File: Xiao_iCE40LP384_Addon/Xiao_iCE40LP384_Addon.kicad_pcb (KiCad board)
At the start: 2 copper layers, 17.8 x 21 mm, 26 parts, among them J1 Conn_01x07_Pin, J2 Conn_01x07_Pin, SW1 SW_Push, U1 ICE40LP384-SG32, U2 ADP322ACPZ-145-R7, U4 XIAO-SAMD21-SMD

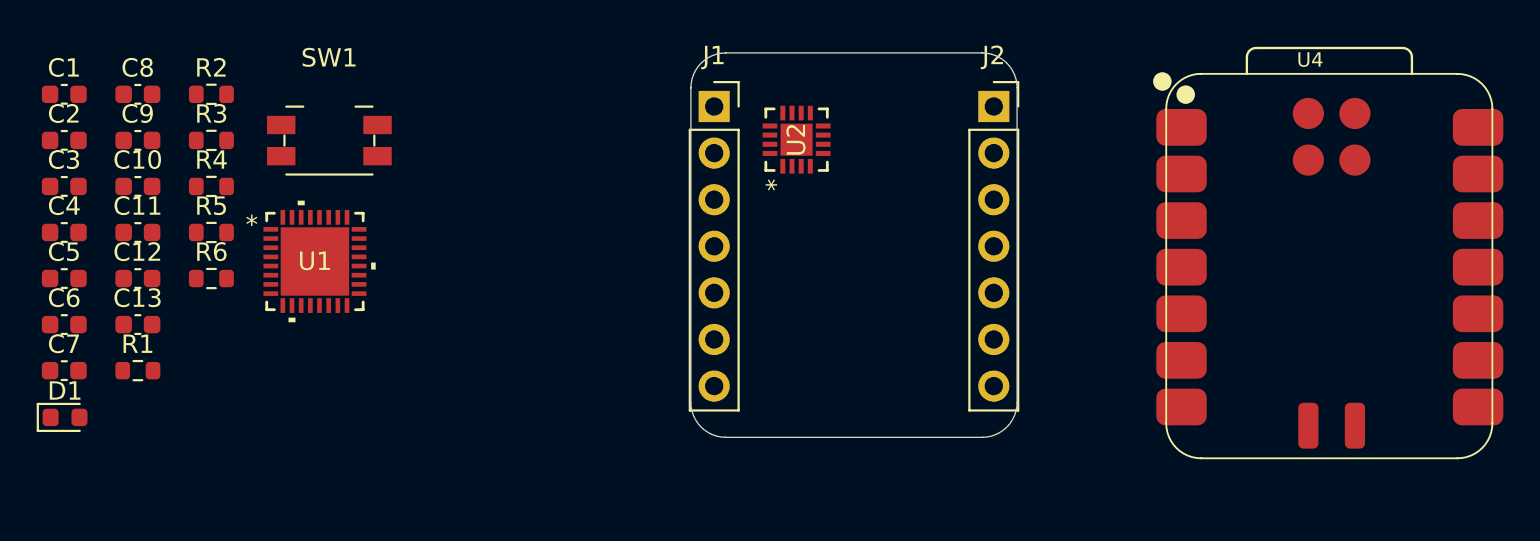
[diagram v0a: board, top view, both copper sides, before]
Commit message: Finished most of the XIAO floorplan, need to route FPGA caps
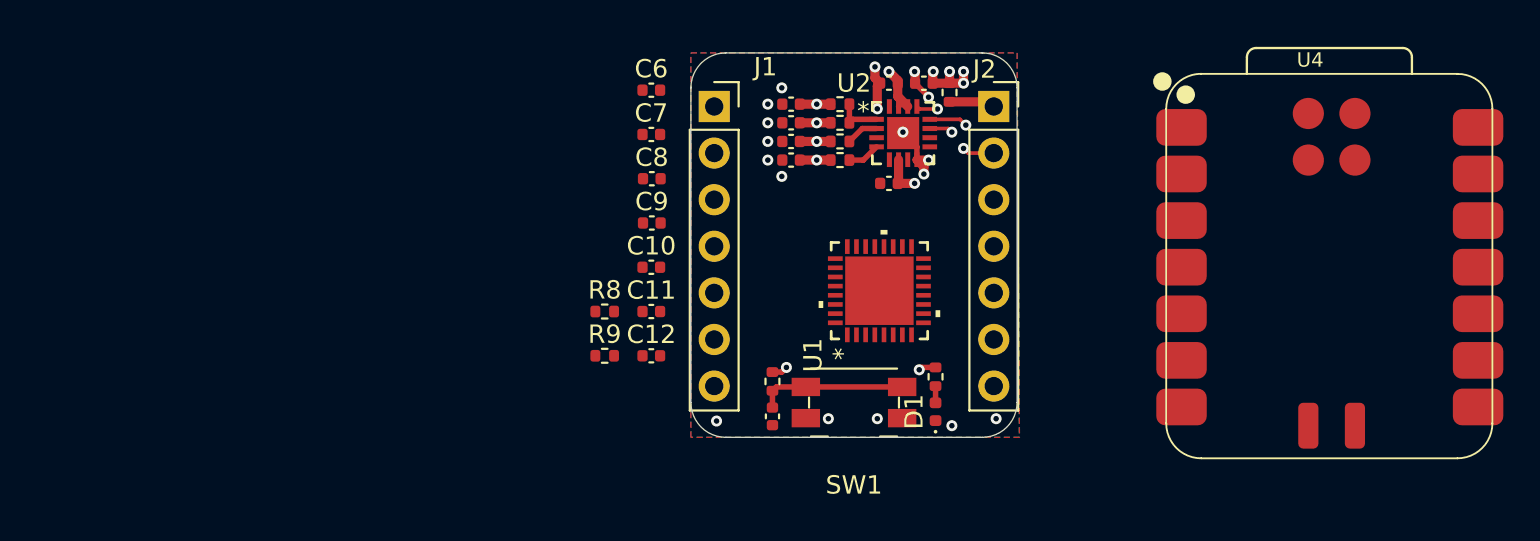
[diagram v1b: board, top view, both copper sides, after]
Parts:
- added C14: 1u, Capacitor_SMD:C_0402_1005Metric, F.Cu at (108.6, 52.1)
- added C15: 100n, Capacitor_SMD:C_0402_1005Metric, F.Cu at (102.2, 70.2)
- added R7: 10k, Resistor_SMD:R_0402_1005Metric, F.Cu at (102.2, 68.3)
- added R8: 0, Resistor_SMD:R_0402_1005Metric, F.Cu at (93.1, 64.5)
- added R9: 0, Resistor_SMD:R_0402_1005Metric, F.Cu at (93.1, 66.9)
- C1, C10, C11, C12, C2, C3, C4, C5, C6, C7, C8, C9: footprint Capacitor_SMD:C_0603_1608Metric -> Capacitor_SMD:C_0402_1005Metric
- C13: value 100n -> 1u; footprint Capacitor_SMD:C_0603_1608Metric -> Capacitor_SMD:C_0402_1005Metric
- D1: footprint LED_SMD:LED_0603_1608Metric -> LED_SMD:LED_0402_1005Metric
- R1, R2, R3, R4: footprint Resistor_SMD:R_0603_1608Metric -> Resistor_SMD:R_0402_1005Metric
- R5: value 1000 -> 0; footprint Resistor_SMD:R_0603_1608Metric -> Resistor_SMD:R_0402_1005Metric
- R6: value 10k -> 1000; footprint Resistor_SMD:R_0603_1608Metric -> Resistor_SMD:R_0402_1005Metric
- moved D1 47.5 mm to (111.1, 70.0), turned to 90 degrees
- moved C1 46.9 mm to (110.5, 52.1), turned to 180 degrees
- moved C13 41.7 mm to (108.6, 57.5), turned to 180 degrees
- moved R5 41.0 mm to (111.9, 52.6), turned to 90 degrees
- moved C5 40.3 mm to (103.3, 55.2), turned to 180 degrees
- moved C4 40.1 mm to (103.3, 54.2), turned to 180 degrees
- moved R1 40.0 mm to (105.9, 56.3), turned to 180 degrees
- moved C3 39.9 mm to (103.3, 53.2), turned to 180 degrees
- moved R6 39.8 mm to (111.1, 68.1), turned to -90 degrees
- moved C2 39.6 mm to (103.3, 56.3), turned to 180 degrees
- moved C7 34.5 mm to (95.6, 54.9)
- moved C6 34.5 mm to (95.6, 52.5)
- moved R4 34.4 mm to (105.9, 55.2), turned to 180 degrees
- moved R3 34.3 mm to (105.9, 54.2), turned to 180 degrees
- moved R2 34.3 mm to (105.9, 53.2), turned to 180 degrees
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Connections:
- C13 pad 1: /CRESET_B -> /5V0
- J1 pad 1: unconnected-(J1-Pin_1-Pad1) -> /D0
- J1 pad 2: unconnected-(J1-Pin_2-Pad2) -> /D1
- J1 pad 3: unconnected-(J1-Pin_3-Pad3) -> /D2
- J1 pad 4: unconnected-(J1-Pin_4-Pad4) -> /D3
- J1 pad 5: unconnected-(J1-Pin_5-Pad5) -> /D4_SDA
- J1 pad 6: unconnected-(J1-Pin_6-Pad6) -> /D5_SCL
- J1 pad 7: unconnected-(J1-Pin_7-Pad7) -> /D6_RX
- J2 pad 1: unconnected-(J2-Pin_1-Pad1) -> /5V0_IN
- J2 pad 2: unconnected-(J2-Pin_2-Pad2) -> /GND
- J2 pad 3: unconnected-(J2-Pin_3-Pad3) -> /3V3_IN
- J2 pad 4: unconnected-(J2-Pin_4-Pad4) -> /D10_MISO
- J2 pad 5: unconnected-(J2-Pin_5-Pad5) -> /D9_MOSI
- J2 pad 6: unconnected-(J2-Pin_6-Pad6) -> /D8_SCK
- J2 pad 7: unconnected-(J2-Pin_7-Pad7) -> /D7_TX
- R5 pad 1: /5V0 -> /5V0_IN
- R5 pad 2: Net-(D1-A) -> /5V0
- R6 pad 1: /VCCIO -> /5V0
- R6 pad 2: /CRESET_B -> Net-(D1-A)
- U1 pad 10: unconnected-(U1-CRESET_B-Pad10) -> /CRESET_B
- U1 pad 11: unconnected-(U1-CDONE-Pad11) -> /CDONE
- U1 pad 12: unconnected-(U1-IOB_24_SDO-Pad12) -> /D9_MOSI
- U1 pad 13: unconnected-(U1-IOB_25_SDI-Pad13) -> /D10_MISO
- U1 pad 15: unconnected-(U1-IOB_26_SCK-Pad15) -> /D8_SCK
- U1 pad 19: unconnected-(U1-IOR_35_GBIN3-Pad19) -> /D5_SCL
- U1 pad 20: unconnected-(U1-IOR_36_GBIN2-Pad20) -> /D4_SDA
- U1 pad 29: unconnected-(U1-IOT_49_GBIN0-Pad29) -> /D2
- U1 pad 30: unconnected-(U1-IOT_50_GBIN1-Pad30) -> /D3
- U1 pad 6: unconnected-(U1-IOL_4B_GBIN7-Pad6) -> /D7_TX
- U1 pad 7: unconnected-(U1-IOL_5A_GBIN6-Pad7) -> /D6_RX
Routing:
- net /5V0: track 0.00 -> 9.53 mm, vias 0 -> 7
- net /GND: track 0.00 -> 9.25 mm, vias 0 -> 19
- net /CRESET_B: track 0.00 -> 8.07 mm
- net /3V3: track 0.00 -> 2.58 mm
- net /VCCIO: track 0.00 -> 2.54 mm, vias 0 -> 2
- net /5V0_IN: track 0.00 -> 2.52 mm
- net /EN2: track 0.00 -> 2.10 mm, vias 0 -> 1
- net /1V2: track 0.00 -> 1.78 mm
- net /2V5: track 0.00 -> 1.77 mm
- net /VCC_SPI: track 0.00 -> 1.68 mm, vias 0 -> 1
- net /VCC: track 0.00 -> 1.68 mm, vias 0 -> 1
- net /VPP: track 0.00 -> 1.52 mm, vias 0 -> 1
- net /EN3: track 0.00 -> 1.29 mm, vias 0 -> 1
- net /EN1: track 0.00 -> 1.18 mm, vias 0 -> 1
- net Net-(D1-A): track 0.00 -> 0.91 mm
- added copper zone on In2.Cu, net /5V0
- added copper zone on B.Cu, net /GND
- added copper zone on F.Cu, net /GND
- added copper zone on In1.Cu, net /GND
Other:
- copper layers 2 -> 4

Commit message: XIAO done, as long as no problems come up during prototype testing
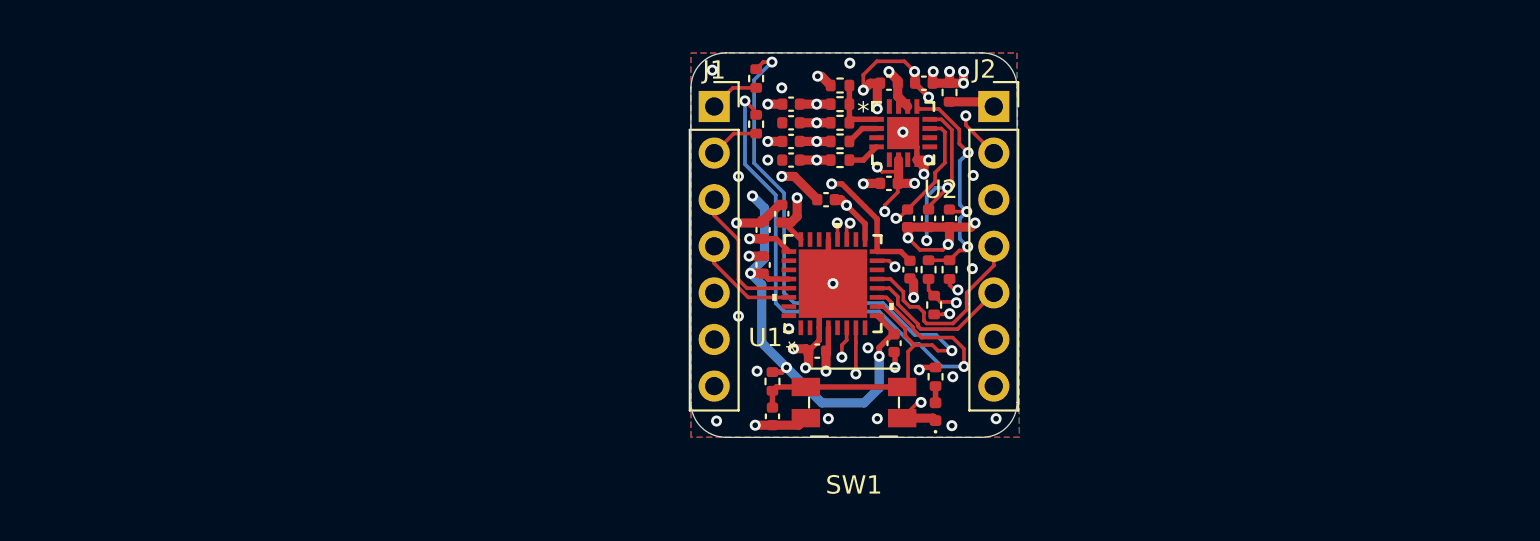
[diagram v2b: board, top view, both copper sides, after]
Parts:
- removed U4: XIAO-SAMD21-SMD, XIAO Footprints and Symbols:XIAO-RP2040-SMD
- added C16: 100n, Capacitor_SMD:C_0402_1005Metric, F.Cu at (109.6, 59.4)
- added C17: 100n, Capacitor_SMD:C_0402_1005Metric, F.Cu at (111.9, 59.4)
- added C18: 100n, Capacitor_SMD:C_0402_1005Metric, F.Cu at (110.7, 59.4)
- added R10: 10k, Resistor_SMD:R_0402_1005Metric, F.Cu at (102.2, 68.3)
- added R11: 10k, Resistor_SMD:R_0402_1005Metric, F.Cu at (111.0, 64.2)
- added R12: 10k, Resistor_SMD:R_0402_1005Metric, F.Cu at (110.7, 62.2)
- added R13: 10k, Resistor_SMD:R_0402_1005Metric, F.Cu at (111.9, 62.2)
- R6: value 1000 -> 0
- R7: value 10k -> 1000
- moved R6 16.7 mm to (105.9, 52.2), turned to 0 degrees
- moved C8 16.0 mm to (108.9, 66.2), turned to -90 degrees
- moved R8 15.1 mm to (101.3, 51.8), turned to -90 degrees
- moved R9 15.1 mm to (101.3, 54.3), turned to -90 degrees
- moved C11 14.3 mm to (109.7, 62.2), turned to -90 degrees
- moved C9 11.4 mm to (104.7, 66.7), turned to 180 degrees
- moved C12 10.5 mm to (102.7, 59.2), turned to 90 degrees
- moved C7 10.2 mm to (105.2, 58.4), turned to 180 degrees
- moved C6 9.76 mm to (101.7, 60.1), turned to 90 degrees
- moved R7 8.89 mm to (111.1, 68.1)
- moved C10 6.10 mm to (101.7, 62.0), turned to 90 degrees
- moved U1 2.56 mm to (105.5, 63.0)
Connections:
- R6 pad 1: /5V0 -> /3V3_IN
- R6 pad 2: Net-(D1-A) -> /3V3
- R7 pad 1: /VCCIO -> /5V0
- R7 pad 2: /CRESET_B -> Net-(D1-A)
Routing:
- net /VCCIO: track 2.54 -> 63.1 mm, vias 2 -> 7
- net /GND: track 9.25 -> 48.0 mm, vias 19 -> 41
- net /CRESET_B: track 8.07 -> 41.1 mm, vias 0 -> 2
- net /CDONE: track 0.00 -> 31.4 mm, vias 0 -> 2
- net /5V0: track 9.53 -> 34.4 mm, vias 7 -> 10
- net /3V3_IN: track 0.00 -> 15.9 mm, vias 0 -> 1
- net /EN3: track 1.29 -> 15.6 mm, vias 1 -> 2
- net /EN2: track 2.10 -> 14.5 mm, vias 1 -> 3
- net /EN1: track 1.18 -> 13.5 mm, vias 1 -> 3
- net /VCC_SPI: track 1.68 -> 13.7 mm, vias 1 -> 2
- net /D5_SCL: track 0.00 -> 11.5 mm, vias 0 -> 1
- net /D6_RX: track 0.00 -> 11.2 mm, vias 0 -> 1
- net /D10_MISO: track 0.00 -> 10.8 mm
- net /D7_TX: track 0.00 -> 10.6 mm, vias 0 -> 1
- net /D4_SDA: track 0.00 -> 9.85 mm, vias 0 -> 1
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- added copper zone on In2.Cu, net /VCCIO

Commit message: Noted lack of 5V tolerance
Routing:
- net /GND: track 48.0 -> 48.4 mm, vias 41 -> 42
- net /VCCIO: vias 7 -> 9
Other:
- board text added: "Not 5V Tolerant!"
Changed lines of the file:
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@@
 	(paper "A4")
 	(layers
-		(0 "F.Cu" signal)
-		(4 "In1.Cu" signal)
-		(6 "In2.Cu" signal)
-		(2 "B.Cu" signal)
+		(0 "F.Cu" mixed)
+		(4 "In1.Cu" power)
+		(6 "In2.Cu" mixed)
+		(2 "B.Cu" power)
 		(9 "F.Adhes" user "F.Adhesive")
 		(11 "B.Adhes" user "B.Adhesive")
@@
 		(layer "Edge.Cuts")
 	)
+	(gr_text "Not 5V Tolerant!"
+		(at 106.7562 51.5874 0)
+		(layer "F.SilkS")
+		(effects
+			(font
+				(size 0.8 0.8)
+				(thickness 0.1)
+			)
+			(justify bottom)
+		)
+	)
 	(segment
 		(start 108.585 51.435)
@@
 	)
 	(via
+		(at 114.5286 51.5874)
+		(size 0.6)
+		(drill 0.3)
+		(layers "F.Cu" "B.Cu")
+		(free yes)
+		(net 2)
+	)
+	(via
 		(at 113.284 59.69)
 		(size 0.6)
@@
 	)
 	(segment
+		(start 102.743 52.324)
+		(end 102.87 52.451)
+		(width 0.2)
+		(layer "B.Cu")
+		(net 2)
+	)
+	(segment
+		(start 102.743 52.324)
+		(end 102.87 52.451)
+		(width 0.2)
+		(layer "In1.Cu")
+		(net 2)
+	)
+	(segment
 		(start 100.9904 60.551)
 		(end 101.727 60.551)
@@
 	)
 	(segment
-		(start 106.0196 57.5564)
-		(end 105.4608 57.5564)
+		(start 107.9373 59.4741)
+		(end 107.9373 59.9593)
 		(width 0.3)
 		(layer "F.Cu")
@@
 	)
 	(segment
-		(start 107.9373 59.4741)
-		(end 106.0196 57.5564)
+		(start 107.9373 59.9593)
+		(end 109.224001 61.246001)
 		(width 0.3)
 		(layer "F.Cu")
@@
 	)
 	(segment
-		(start 107.9373 61.246001)
-		(end 107.9373 59.4741)
+		(start 105.664 57.5564)
+		(end 106.0196 57.5564)
 		(width 0.3)
 		(layer "F.Cu")
@@
 	)
 	(segment
+		(start 106.0196 57.5564)
+		(end 107.9373 59.4741)
+		(width 0.3)
+		(layer "F.Cu")
+		(net 4)
+	)
+	(segment
 		(start 104.648 53.213)
 		(end 105.408 53.213)
@@
 	)
 	(via
-		(at 105.4608 57.5564)
+		(at 105.664 57.5564)
 		(size 0.6)
 		(drill 0.3)
@@
 	)
 	(segment
-		(start 105.4608 57.5564)
-		(end 105.664 57.3532)
+		(start 104.9274 53.213)
+		(end 104.648 53.213)
 		(width 0.5)
 		(layer "In2.Cu")
@@
 	)
 	(segment
-		(start 105.664 57.3532)
+		(start 105.664 57.5564)
 		(end 105.664 53.9496)
 		(width 0.5)
@@
 	)
 	(segment
-		(start 104.9274 53.213)
-		(end 104.648 53.213)
-		(width 0.5)
-		(layer "In2.Cu")
-		(net 4)
-	)
-	(segment
 		(start 105.283 65.4003)
 		(end 105.283 66.548)
@@
 	)
 	(via
+		(at 101.6508 64.4652)
+		(size 0.6)
+		(drill 0.3)
+		(layers "F.Cu" "B.Cu")
+		(net 5)
+	)
+	(via
 		(at 101.0412 62.4332)
 		(size 0.6)
@@
 		(net 5)
 	)
+	(via
+		(at 106.7308 69.4944)
+		(size 0.6)
+		(drill 0.3)
+		(layers "F.Cu" "B.Cu")
+		(net 5)
+	)
+	(segment
+		(start 106.7308 69.4944)
+		(end 104.9274 69.4944)
+		(width 0.5)
+		(layer "B.Cu")
+		(net 5)
+	)
 	(segment
 		(start 104.9274 69.4944)
@@
 	(segment
 		(start 101.6508 66.2178)
+		(end 101.6508 64.4652)
+		(width 0.5)
+		(layer "B.Cu")
+		(net 5)
+	)
+	(segment
+		(start 101.6508 64.4652)
 		(end 101.6508 63.0428)
 		(width 0.5)
@@
 	(segment
 		(start 107.2388 69.4944)
-		(end 104.9274 69.4944)
+		(end 106.7308 69.4944)
 		(width 0.5)
 		(layer "B.Cu")
@@
 		(start 111.887 53.086)
 		(end 114.046 53.086)
-		(width 0.5)
+		(width 0.6)
 		(layer "F.Cu")
 		(net 41)
@@
 		(hatch edge 0.5)
 		(connect_pads
-			(clearance 0.5)
+			(clearance 0.2)
 		)
 		(min_thickness 0.25)
@@
 		(priority 2)
 		(connect_pads
-			(clearance 0.5)
+			(clearance 0.2)
 		)
 		(min_thickness 0.25)
@@
 		(priority 1)
 		(connect_pads
-			(clearance 0.5)
+			(clearance 0.2)
 		)
 		(min_thickness 0.25)

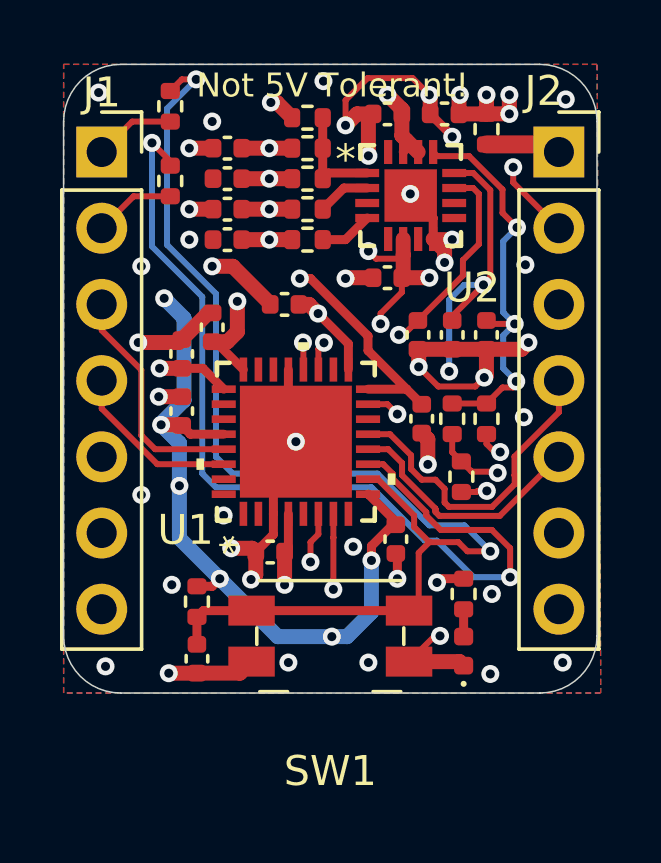
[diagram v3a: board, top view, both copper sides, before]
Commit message: Improve silkscreen, fix ADP322 footprint error
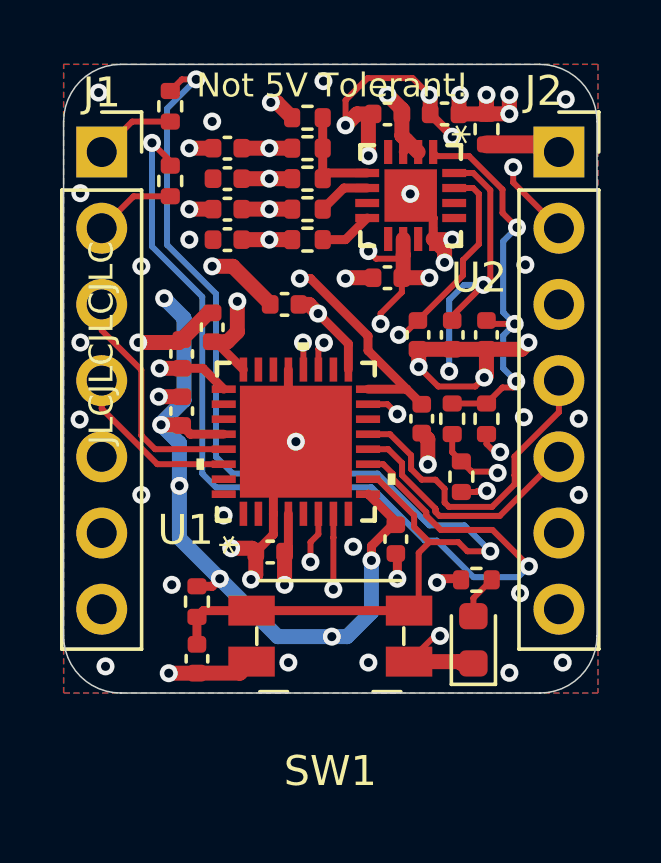
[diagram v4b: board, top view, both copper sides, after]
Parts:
- D1: footprint LED_SMD:LED_0402_1005Metric -> LED_SMD:LED_0603_1608Metric
- moved R7 0.64 mm to (111.5, 67.6), turned to 0 degrees
- moved D1 0.50 mm to (111.5, 69.6)
- turned U2 to -90 degrees
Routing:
- net /CDONE: track 31.4 -> 32.1 mm
- net Net-(D1-A): track 0.91 -> 1.47 mm
- net /GND: track 48.4 -> 48.7 mm, vias 42 -> 47
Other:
- board text added: "5V0 GND 3V3 D10 D9 D8 D7"
- board text added: "D0 D1 D2 D3 D4 D5 D6"
- board text added: "JLCJLCJLCJLC"
- board text added: "Top Hat Hardware Co."

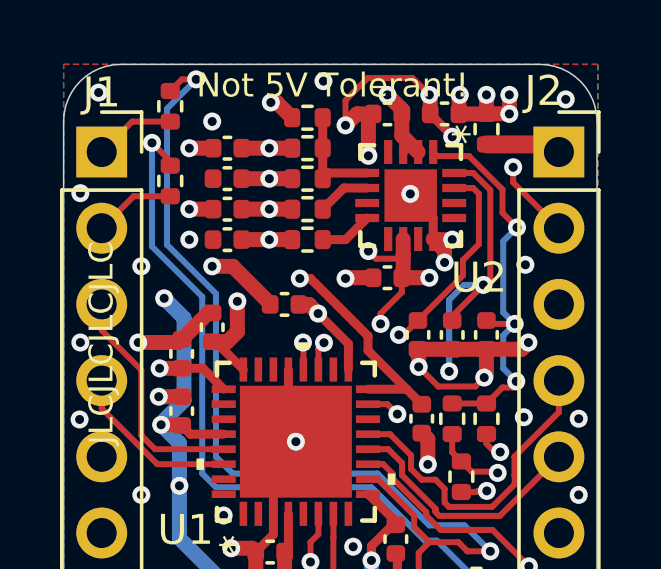
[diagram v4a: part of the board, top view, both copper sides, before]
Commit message: Slow down RC timer and add test points to power supply
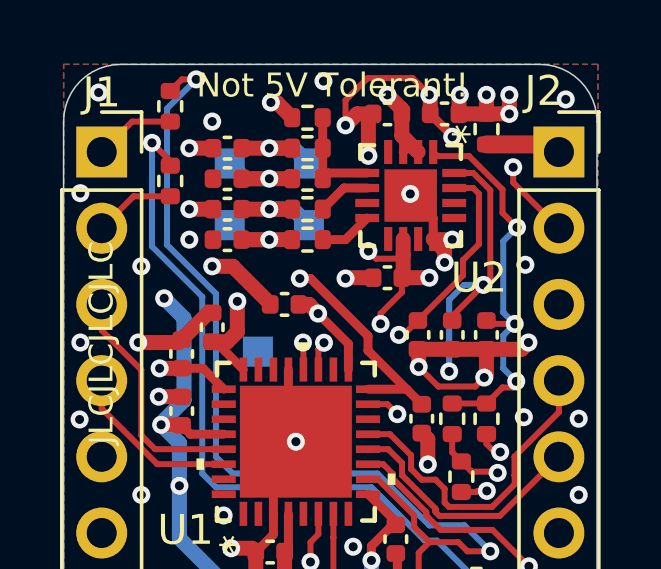
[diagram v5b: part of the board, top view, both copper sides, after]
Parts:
- added TP1: TestPoint, TestPoint:TestPoint_Pad_1.0x1.0mm, B.Cu at (103.3, 55.8)
- added TP2: TestPoint, TestPoint:TestPoint_Pad_1.0x1.0mm, B.Cu at (106.0, 53.7)
- added TP3: TestPoint, TestPoint:TestPoint_Pad_1.0x1.0mm, B.Cu at (103.3, 53.7)
- added TP4: TestPoint, TestPoint:TestPoint_Pad_1.0x1.0mm, B.Cu at (106.0, 55.8)
- added TP5: TestPoint, TestPoint:TestPoint_Pad_1.0x1.0mm, B.Cu at (104.3, 60.0)
- C16, C17, C18: value 100n -> 4.7u
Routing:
- net /VPP: track 8.45 -> 9.99 mm
- net /VCC_SPI: track 14.0 -> 15.5 mm
- net /VCCIO: track 63.1 -> 64.7 mm
- net /VCC: track 10.8 -> 12.3 mm
